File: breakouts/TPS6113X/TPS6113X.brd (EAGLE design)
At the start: 13 x 21 mm, 7 parts

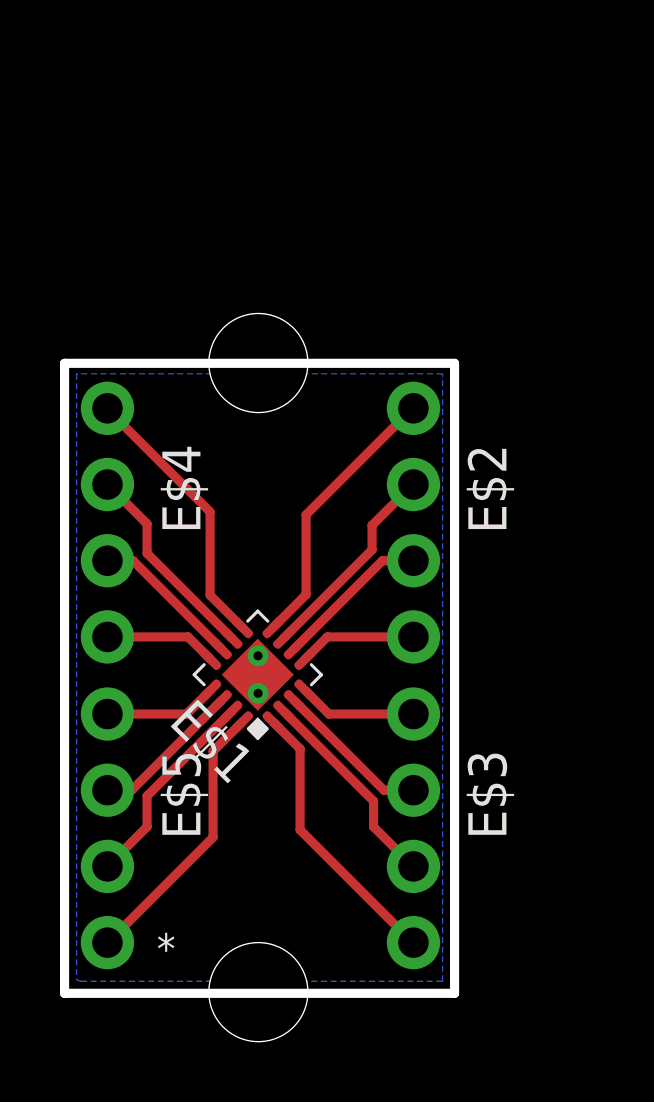
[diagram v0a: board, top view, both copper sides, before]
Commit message: update t-silk to include package and IC name
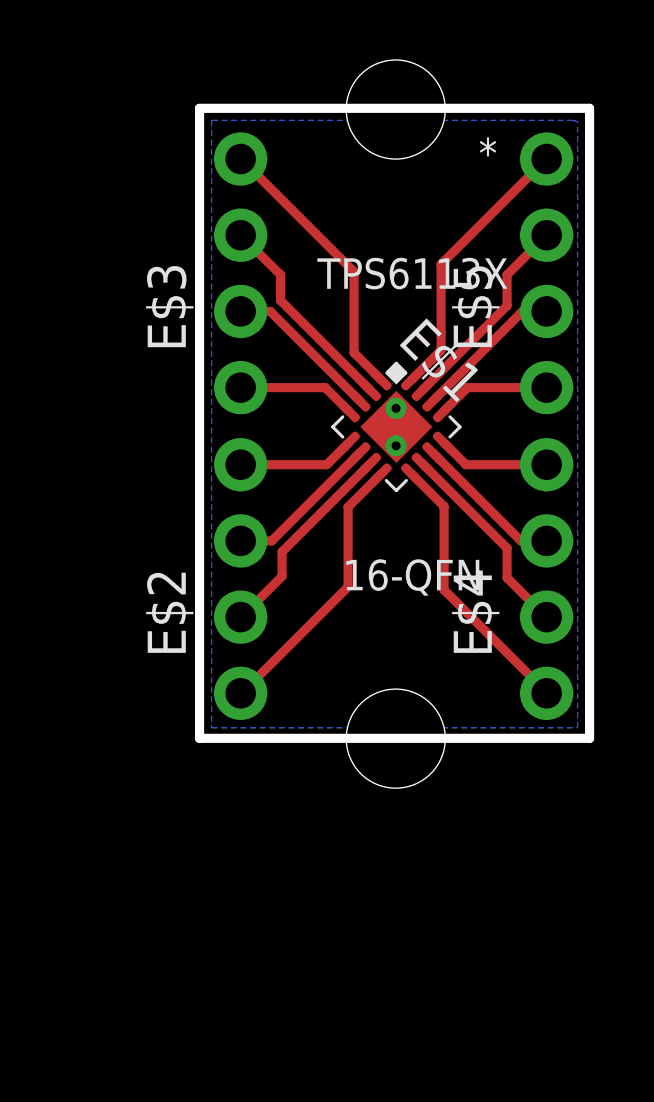
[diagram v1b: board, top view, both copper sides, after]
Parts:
- moved JP3 29.8 mm to (13.5, 31.8), turned to 90 degrees
- moved E$5 23.6 mm to (18.6, 26.3), turned to 90 degrees
- moved E$3 19.4 mm to (8.37, 26.3), turned to 90 degrees
- moved E$4 14.8 mm to (18.6, 16.1), turned to 90 degrees
- moved JP4 13.3 mm to (13.5, 10.8), turned to 90 degrees
- moved E$1 9.46 mm to (13.6, 21.2), turned to 315 degrees
- moved E$2 6.06 mm to (8.37, 16.1), turned to 90 degrees
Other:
- board text added: "16-QFN"
- board text added: "TPS6113X"
